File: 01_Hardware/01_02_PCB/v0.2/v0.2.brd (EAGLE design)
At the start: 160 x 100 mm, 57 parts

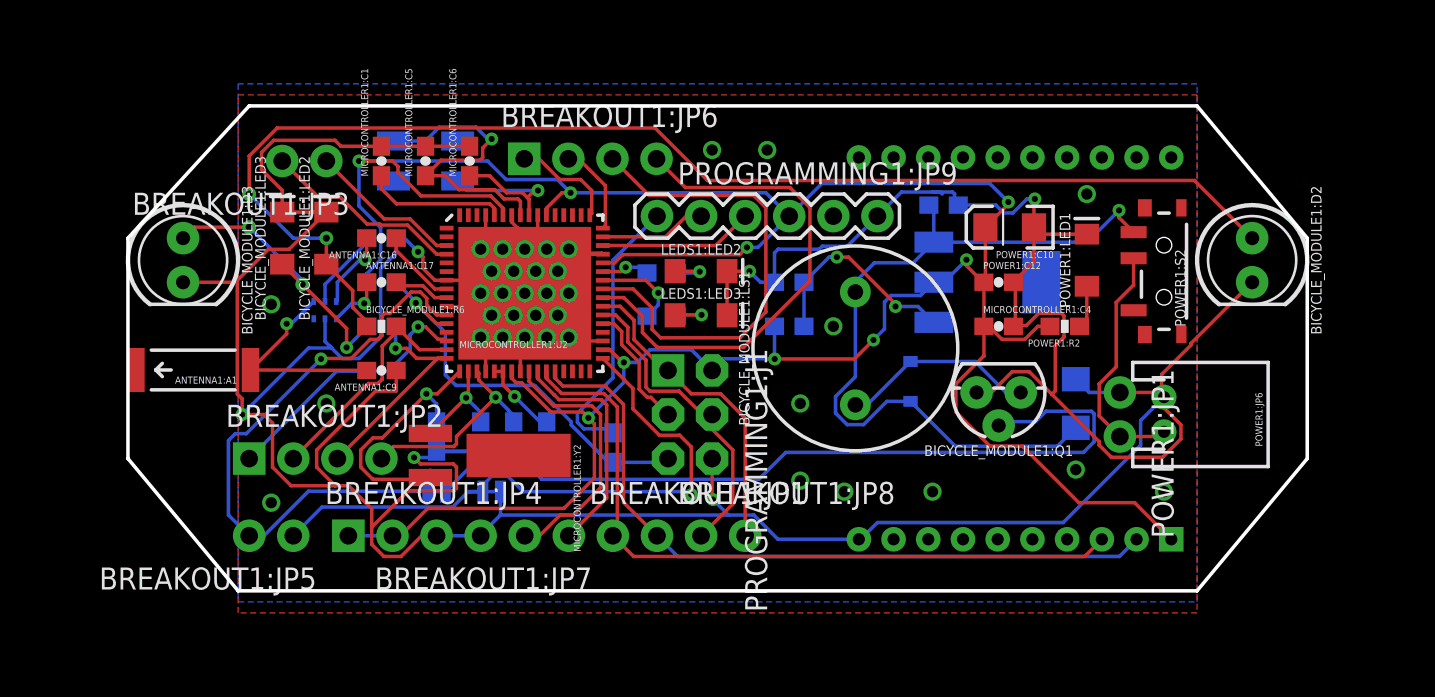
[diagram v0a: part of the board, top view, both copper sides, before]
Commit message: 3v3 reg uptE
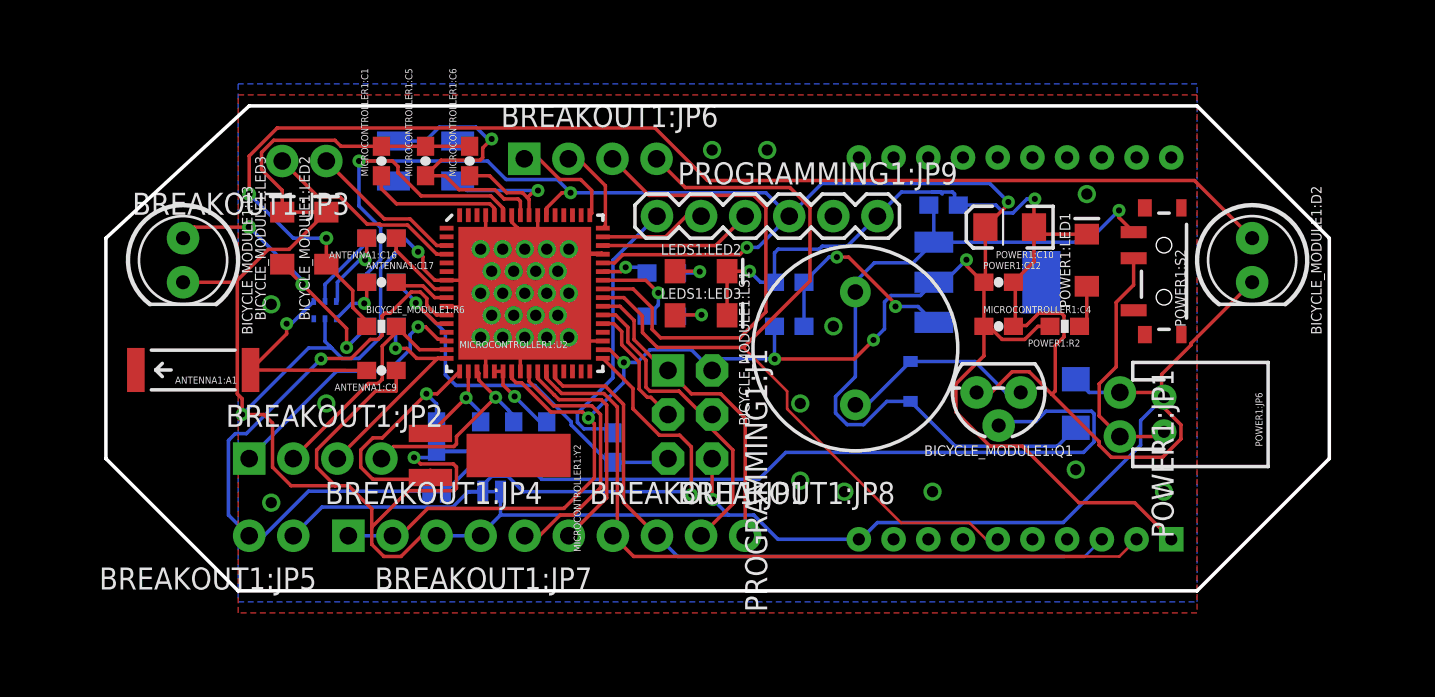
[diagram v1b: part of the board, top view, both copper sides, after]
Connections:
- net PB4: now also BREAKOUT1:U$2.6
- net RX1: now also BREAKOUT1:U$2.2; no longer BREAKOUT1:U$2.3
- net TX1: now also BREAKOUT1:U$2.3; no longer BREAKOUT1:U$2.2
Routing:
- net PB4: track 29.5 -> 49.3 mm
- net TX1: track 41.9 -> 39.9 mm
- net RX1: track 41.8 -> 43.8 mm
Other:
- outline, holes or cut-outs redrawn
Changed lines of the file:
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@@
 <wire x1="0" y1="100" x2="0" y2="0" width="0" layer="20"/>
 <wire x1="32.385" y1="59.055" x2="86.995" y2="59.055" width="0.2032" layer="20"/>
-<wire x1="86.995" y1="59.055" x2="93.345" y2="51.435" width="0.2032" layer="20"/>
-<wire x1="93.345" y1="51.435" x2="93.345" y2="38.735" width="0.2032" layer="20"/>
-<wire x1="93.345" y1="38.735" x2="86.995" y2="31.115" width="0.2032" layer="20"/>
+<wire x1="86.995" y1="59.055" x2="94.615" y2="51.435" width="0.2032" layer="20"/>
+<wire x1="94.615" y1="51.435" x2="94.615" y2="38.735" width="0.2032" layer="20"/>
+<wire x1="94.615" y1="38.735" x2="86.995" y2="31.115" width="0.2032" layer="20"/>
 <wire x1="86.995" y1="31.115" x2="31.75" y2="31.115" width="0.2032" layer="20"/>
-<wire x1="31.75" y1="31.115" x2="25.4" y2="38.735" width="0.2032" layer="20"/>
-<wire x1="25.4" y1="38.735" x2="25.4" y2="51.435" width="0.2032" layer="20"/>
-<wire x1="25.4" y1="51.435" x2="32.385" y2="59.055" width="0.2032" layer="20"/>
-<dimension x1="32.385" y1="59.055" x2="32.385" y2="31.115" x3="15.24" y3="45.085" textsize="1.778" layer="20" unit="inch"/>
-<dimension x1="86.995" y1="59.055" x2="86.995" y2="31.115" x3="100.965" y3="45.085" textsize="1.778" layer="20" unit="inch"/>
-<dimension x1="25.4" y1="51.435" x2="93.345" y2="51.435" x3="59.3725" y3="62.23" textsize="1.778" layer="20" unit="inch"/>
-<dimension x1="25.4" y1="38.1" x2="31.75" y2="38.1" x3="28.575" y3="24.13" textsize="1.778" layer="20" unit="inch"/>
-<dimension x1="93.98" y1="51.435" x2="93.98" y2="38.735" x3="97.155" y3="45.085" textsize="1.778" layer="20" unit="inch"/>
-<dimension x1="25.4" y1="38.735" x2="25.4" y2="51.435" x3="21.59" y3="45.085" textsize="1.778" layer="20" unit="inch"/>
-<dimension x1="93.345" y1="51.435" x2="86.995" y2="51.435" x3="90.17" y3="23.495" textsize="1.778" layer="20" unit="inch"/>
-<dimension x1="25.4" y1="51.435" x2="25.4" y2="59.055" x3="17.78" y3="55.245" textsize="1.778" layer="20" unit="inch"/>
-<dimension x1="93.345" y1="51.435" x2="93.345" y2="59.055" x3="99.06" y3="55.245" textsize="1.778" layer="20" unit="inch"/>
+<wire x1="31.75" y1="31.115" x2="24.13" y2="38.735" width="0.2032" layer="20"/>
+<wire x1="24.13" y1="38.735" x2="24.13" y2="51.435" width="0.2032" layer="20"/>
+<wire x1="24.13" y1="51.435" x2="32.385" y2="59.055" width="0.2032" layer="20"/>
 </plain>
 <attributes>
@@
 <contactref element="MICROCONTROLLER1:U2" pad="28"/>
 <contactref element="BREAKOUT1:JP1" pad="2"/>
-<contactref element="BREAKOUT1:U$2" pad="2"/>
 <wire x1="55.88" y1="34.29" x2="57.0738" y2="33.0962" width="0.2032" layer="16"/>
 <wire x1="50.2676" y1="43.106" x2="50.2647875" y2="43.106" width="0.2032" layer="1"/>
@@
 <wire x1="50.2676" y1="43.106" x2="50.4587" y2="42.9149" width="0.2032" layer="1"/>
 <wire x1="50.4587" y1="42.9149" x2="52.8939" y2="42.9149" width="0.2032" layer="1"/>
-<wire x1="82.5212" y1="33.0962" x2="83.51" y2="34.085" width="0.2032" layer="16"/>
-<wire x1="57.0738" y1="33.0962" x2="82.5212" y2="33.0962" width="0.2032" layer="16"/>
+<wire x1="79.375" y1="33.0962" x2="57.0738" y2="33.0962" width="0.2032" layer="16"/>
 <wire x1="53.95215" y1="41.85665" x2="53.95215" y2="36.21785" width="0.2032" layer="1"/>
 <wire x1="52.8939" y1="42.9149" x2="53.95215" y2="41.85665" width="0.2032" layer="1"/>
 <wire x1="53.95215" y1="36.21785" x2="55.88" y2="34.29" width="0.2032" layer="1"/>
+<contactref element="BREAKOUT1:U$2" pad="3"/>
+<wire x1="81.51" y1="34.085" x2="80.5212" y2="33.0962" width="0.1524" layer="16"/>
+<wire x1="80.5212" y1="33.0962" x2="79.375" y2="33.0962" width="0.1524" layer="16"/>
 </signal>
 <signal name="RX1">
 <contactref element="MICROCONTROLLER1:U2" pad="27"/>
 <contactref element="BREAKOUT1:JP1" pad="1"/>
-<contactref element="BREAKOUT1:U$2" pad="3"/>
 <wire x1="53.34" y1="34.29" x2="54.5338" y2="33.0962" width="0.2032" layer="1"/>
 <wire x1="50.1203" y1="42.7504" x2="50.1174875" y2="42.7504" width="0.2032" layer="1"/>
@@
 <wire x1="50.38505" y1="42.48565" x2="52.82025" y2="42.48565" width="0.2032" layer="1"/>
 <wire x1="52.82025" y1="42.48565" x2="53.59655" y2="41.70935" width="0.2032" layer="1"/>
-<wire x1="81.51" y1="34.085" x2="80.5212" y2="33.0962" width="0.2032" layer="1"/>
-<wire x1="80.5212" y1="33.0962" x2="54.5338" y2="33.0962" width="0.2032" layer="1"/>
+<wire x1="54.5338" y1="33.0962" x2="80.5212" y2="33.0962" width="0.2032" layer="1"/>
 <wire x1="53.59655" y1="34.54655" x2="53.34" y2="34.29" width="0.2032" layer="1"/>
 <wire x1="53.59655" y1="41.70935" x2="53.59655" y2="34.54655" width="0.2032" layer="1"/>
+<contactref element="BREAKOUT1:U$2" pad="2"/>
+<wire x1="80.5212" y1="33.0962" x2="82.5212" y2="33.0962" width="0.1524" layer="1"/>
+<wire x1="82.5212" y1="33.0962" x2="83.51" y2="34.085" width="0.1524" layer="1"/>
 </signal>
 <signal name="SDA">
@@
 <wire x1="53.975" y1="48.01" x2="55.0418" y2="46.9432" width="0.2032" layer="1"/>
 <wire x1="55.0418" y1="46.9432" x2="55.0418" y2="45.9994" width="0.2032" layer="1"/>
-<wire x1="60.8584" y1="45.1358" x2="55.9054" y2="45.1358" width="0.2032" layer="1"/>
+<wire x1="55.9054" y1="45.1358" x2="60.8584" y2="45.1358" width="0.2032" layer="1"/>
 <wire x1="55.0418" y1="45.9994" x2="55.9054" y2="45.1358" width="0.2032" layer="1"/>
 <wire x1="63.544046875" y1="54.349246875" x2="57.512353125" y2="54.349246875" width="0.2032" layer="1"/>
@@
 <wire x1="64.6938" y1="53.19949375" x2="64.6938" y2="48.9712" width="0.2032" layer="1"/>
 <wire x1="64.6938" y1="48.9712" x2="60.8584" y2="45.1358" width="0.2032" layer="1"/>
+<contactref element="BREAKOUT1:U$2" pad="6"/>
+<wire x1="60.8584" y1="45.1358" x2="63.3782" y2="42.616" width="0.1524" layer="1"/>
+<wire x1="74.83908125" y1="34.085" x2="75.51" y2="34.085" width="0.1524" layer="1"/>
+<wire x1="63.3782" y1="42.616" x2="63.3782" y2="41.59651875" width="0.1524" layer="1"/>
+<wire x1="73.89928125" y1="35.0248" x2="74.83908125" y2="34.085" width="0.1524" layer="1"/>
+<wire x1="63.3782" y1="41.59651875" x2="69.94991875" y2="35.0248" width="0.1524" layer="1"/>
+<wire x1="69.94991875" y1="35.0248" x2="73.89928125" y2="35.0248" width="0.1524" layer="1"/>
 </signal>
 <signal name="SSN">
